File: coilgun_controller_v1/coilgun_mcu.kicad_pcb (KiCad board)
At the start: 4 copper layers, 50.8 x 34.6 mm, 32 parts, among them J1 Conn_01x08, J2 Conn_01x05, J3 400V_GENERATOR_VIN, J4 BAT_IN, J5 3V3PWR, J6 3V3, J7 Conn_02x04_Odd_Even, J8 Conn_01x08, SW1 SW_TRIGGER_CHARGE, SW2 SW_TRIGGER_FIRE, SW3 SW_SAFETY, U1 STM32F072CBTx, U2 TLP185, U3 SPAN02A-03, U4 AMSRI-78-NZ, U5 TLP291-4, U6 TLP291-4

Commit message: Increase track clearance, cosmetic fixes
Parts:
- renumbered C6 to C4, C4 to C5, C5 to C6, J7 to J1, J1 to J2, J8 to J3, J2 to J4, J3 to J5, J4 to J6, J5 to J7, J6 to J8, R8 to R2, R9 to R3, R10 to R4, R11 to R5, R12 to R6, R13 to R7, R14 to R8, R15 to R9, SW2 to SW1, SW1 to SW2
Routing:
- net SENS2: track 13.3 -> 14.4 mm
- net TRIGGER: track 10.5 -> 9.57 mm
- net SENS3: track 10.2 -> 11.1 mm
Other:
- copper layers 4 -> 2
- net class Default: clearance 0.1 -> 0.127
- rule trace_clearance: 0.1 -> 0.127
- board text added: "↑ ESP8266 ↑"
- board text removed: "ESP8266"

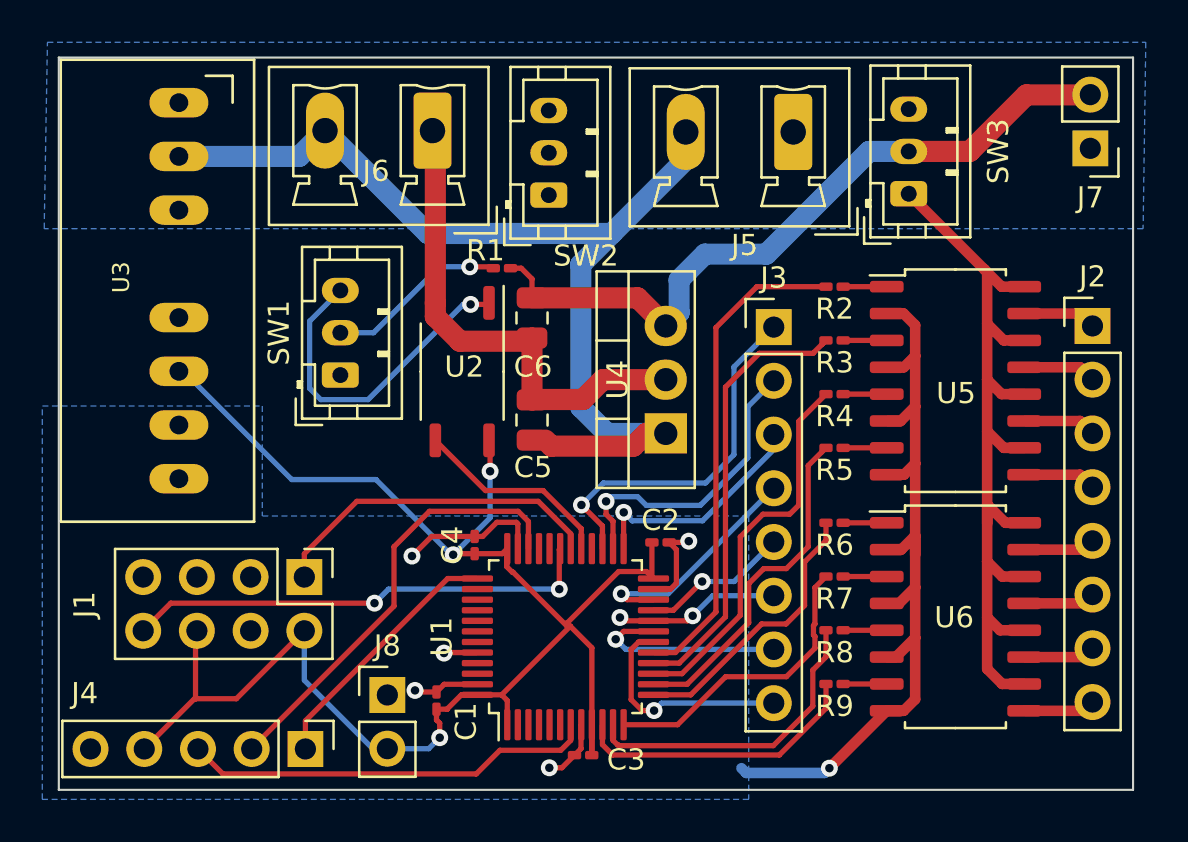
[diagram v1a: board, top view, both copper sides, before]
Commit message: Get rid of the useless optocoupler
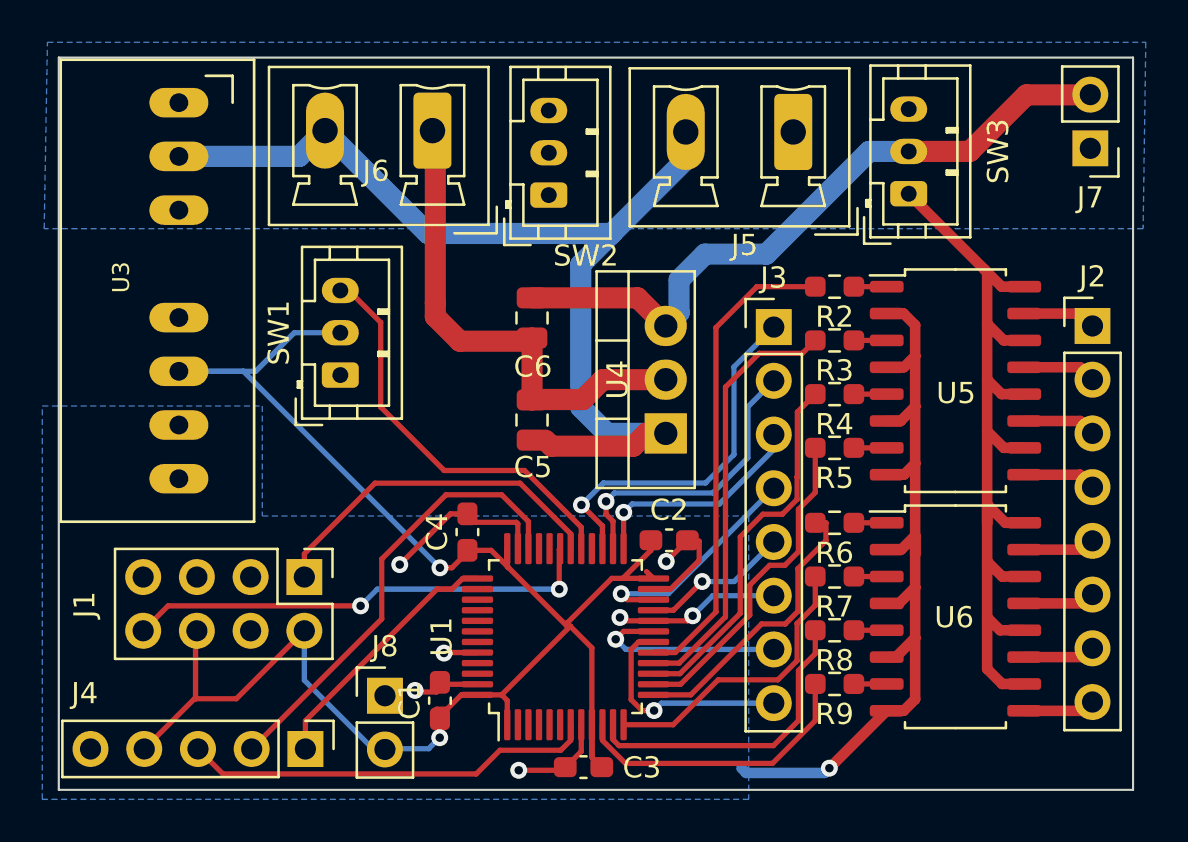
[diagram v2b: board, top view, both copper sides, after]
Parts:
- removed R1: 220, Resistor_SMD:R_0201_0603Metric_Pad0.64x0.40mm_HandSolder
- removed U2: TLP185, Package_SO:SOIC-4_4.55x3.7mm_P2.54mm
- C1, C2, C3, C4: footprint Capacitor_SMD:C_0201_0603Metric_Pad0.64x0.40mm_HandSolder -> Capacitor_SMD:C_0603_1608Metric_Pad1.08x0.95mm_HandSolder
- R2, R3, R4, R5, R6, R7, R8, R9: footprint Resistor_SMD:R_0201_0603Metric_Pad0.64x0.40mm_HandSolder -> Resistor_SMD:R_0603_1608Metric_Pad0.98x0.95mm_HandSolder
- moved C4 0.70 mm to (122.9, 99.6)
- moved C3 0.57 mm to (128.4, 110.7)
- moved C2 0.42 mm to (132.4, 100.0)
- moved C1 0.16 mm to (121.6, 107.5)
- moved J8 0.12 mm to (119.0, 107.3)
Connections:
- SW1 pad 2: Net-(R1-Pad1) -> +3V3
- SW1 pad 3: Net-(SW1-Pad3) -> TRIGGER
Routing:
- net Net-(SW1-Pad3): track 15.8 -> 0.00 mm, vias 1 -> 0
- net TRIGGER: track 9.57 -> 19.6 mm
- net Net-(R1-Pad1): track 8.55 -> 0.00 mm, vias 1 -> 0
- net +3V3: track 80.7 -> 85.5 mm, vias 3 -> 2
- net GND: track 59.3 -> 63.6 mm
- net +3.3VP: track 34.0 -> 31.9 mm
- net TXD: track 16.1 -> 16.8 mm
- net SWDIO: track 20.9 -> 21.5 mm
- net TRIG4: track 16.1 -> 15.5 mm
- net TRIG1: track 23.2 -> 22.7 mm
- net Net-(R9-Pad1): track 2.06 -> 1.55 mm
- net Net-(R8-Pad1): track 2.06 -> 1.55 mm
- net Net-(R7-Pad1): track 2.06 -> 1.55 mm
- net Net-(R6-Pad1): track 2.06 -> 1.55 mm
- net Net-(R5-Pad1): track 2.06 -> 1.55 mm
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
